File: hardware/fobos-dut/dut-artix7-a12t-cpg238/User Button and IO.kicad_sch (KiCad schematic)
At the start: 26 parts

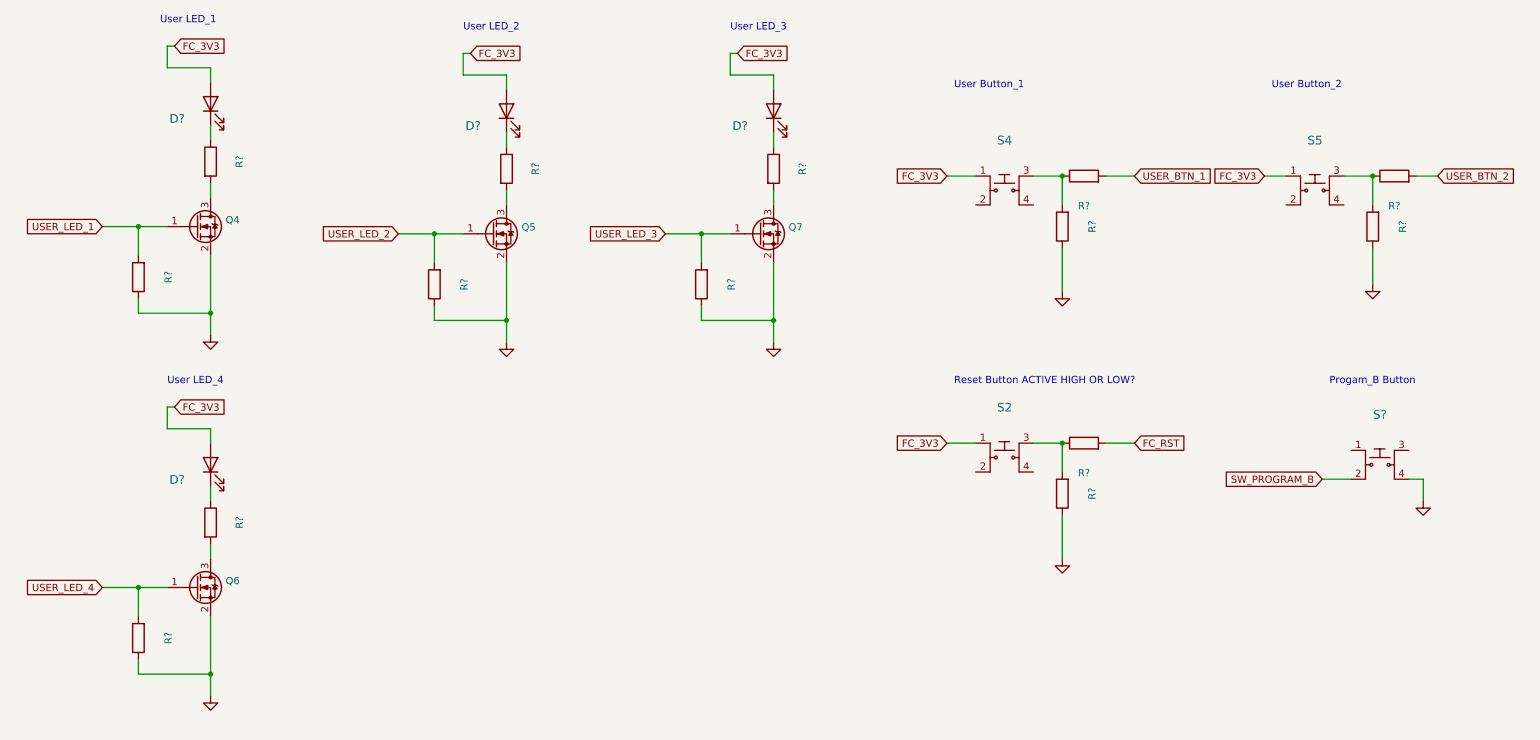
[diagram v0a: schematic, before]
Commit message: transitioned artix-7 dut to Kikad 6
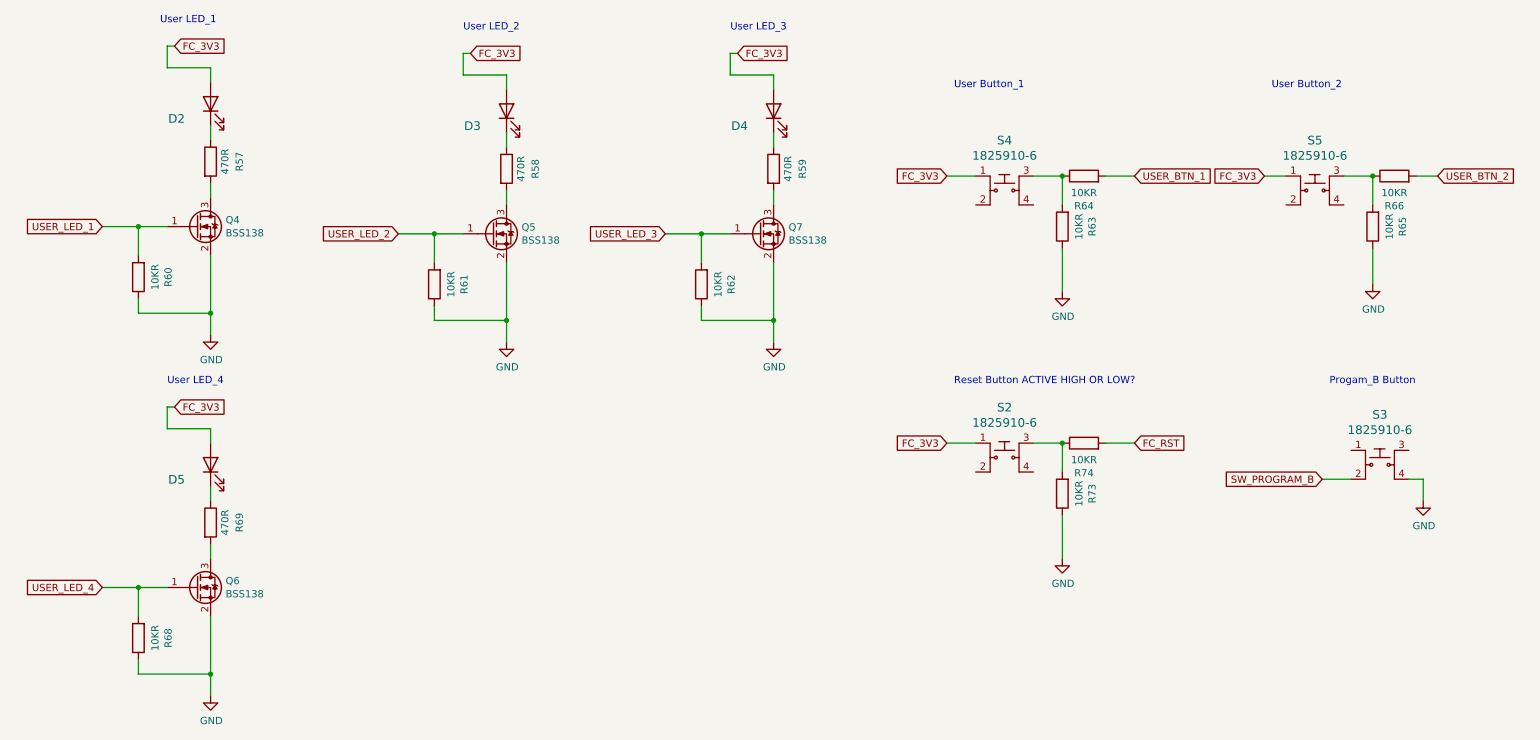
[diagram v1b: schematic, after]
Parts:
- D2, D3, D4, D5: renamed from D?; value (none) -> LG_L29K-G2J1-24-Z; footprint (none) -> LED_SMD:LED_0603_1608Metric
- Q4, Q5, Q6, Q7: value (none) -> BSS138; footprint (none) -> Package_TO_SOT_SMD:SOT-23
- R57, R58, R59, R69: renamed from R?; value (none) -> 470R; footprint (none) -> Resistor_SMD:R_0603_1608Metric
- R60, R61, R62, R63, R64, R65, R66, R68, R73, R74: renamed from R?; value (none) -> 10KR; footprint (none) -> Resistor_SMD:R_0603_1608Metric
- S2, S4, S5: value (none) -> 1825910-6; footprint (none) -> cerg:Switch_Tactile_THT_6x6mm
- S3: renamed from S?; value (none) -> 1825910-6; footprint (none) -> cerg:Switch_Tactile_THT_6x6mm
